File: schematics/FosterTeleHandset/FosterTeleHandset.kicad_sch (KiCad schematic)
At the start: 7 parts, among them Q1 2N2222, U1 US1881EUA-AAA-000-BU

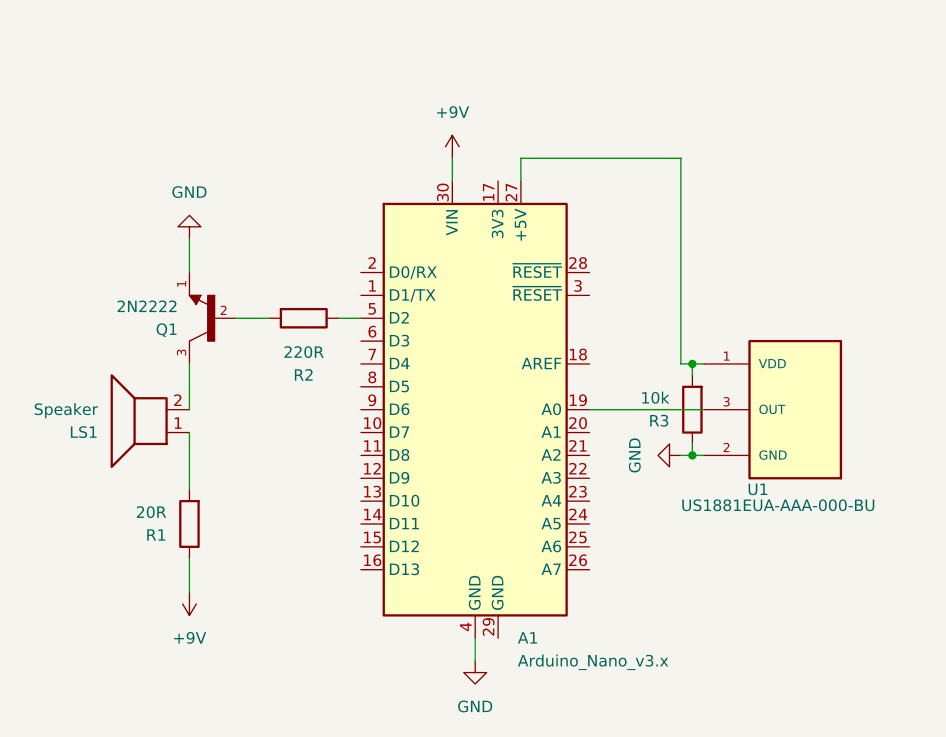
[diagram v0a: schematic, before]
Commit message: Updated circuit diagram to use RP2040 Pico
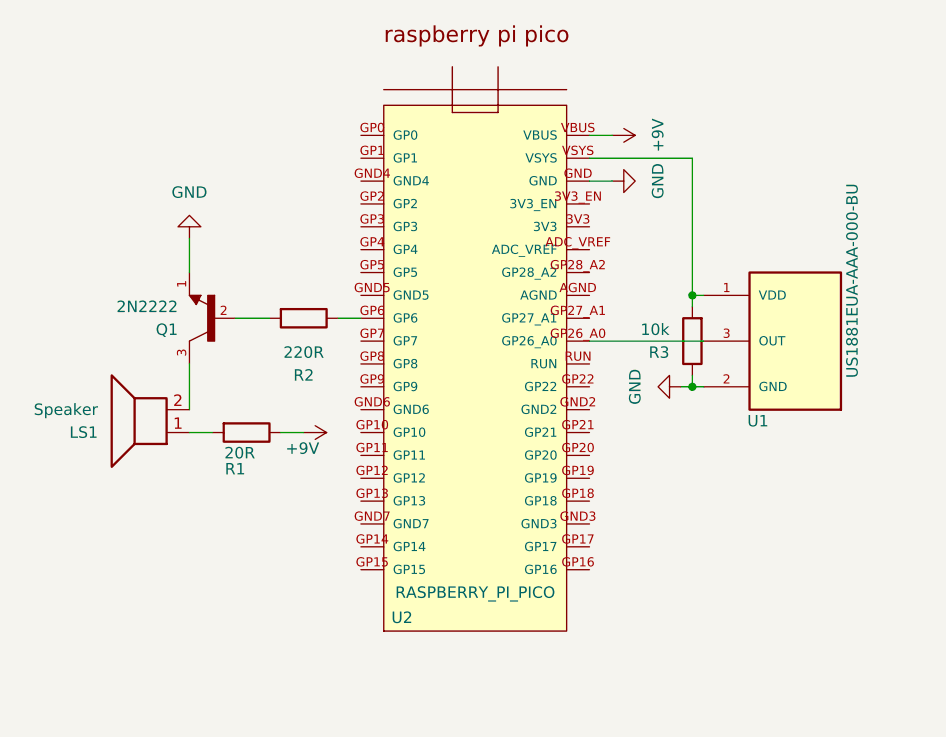
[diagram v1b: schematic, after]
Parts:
- removed A1: Arduino_Nano_v3.x, Module:Arduino_Nano, symbol MCU_Module:Arduino_Nano_v3.x
- added U2: RASPBERRY_PI_PICO, RASPBERRY_PI_PICO:RASPBERRY_PI_PICO, symbol RASPBERRY_PI_PICO:RASPBERRY_PI_PICO
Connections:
- net +9V: now also U2.VBUS
- net GND: now also U2.GND
- net at U1.3 (OUT): now also U2.GP26_A0
- net at R3.2, U1.1 (VDD): now also U2.VSYS
- net at R2.1: now also U2.GP6
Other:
- moved on the sheet: R1, R3, U1

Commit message: Adjusted schematic.
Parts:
- removed LS1: Speaker, symbol Device:Speaker
- removed Q1: 2N2222, 2N2222:TO127P584H533-3, symbol 2N2222:2N2222
- removed R1: 20R, symbol Device:R
- removed R2: 220R, symbol Device:R
- removed R3: 10k, symbol Device:R
- added BZ1: Buzzer, symbol Device:Buzzer
- added J1: Battery Conn, symbol Connector:Conn_01x02_Pin
- U1: value US1881EUA-AAA-000-BU -> US1881
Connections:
- net at U1.1 (VDD): now also U2.GP27_A1; no longer U2.VSYS
- net at U2.GND4: now also BZ1.2 (-)
- net at U2.GP2: now also BZ1.1 (+)
- net +9V: no longer names the net of U2.VBUS
- net GND: no longer names the net of U1.2 (GND), U2.GND
- net GND: now also J1.2 (Pin_2)
- new net: J1.1 (Pin_1), U2.VSYS
